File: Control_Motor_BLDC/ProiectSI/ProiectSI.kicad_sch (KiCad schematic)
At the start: 72 parts, among them J1 Screw_Terminal_01x05, J2 Conn_01x04_Pin, J3 Screw_Terminal_01x03, J5 Conn_01x02_Pin, Q1 NMOS_Substrate, Q2 NMOS_Substrate, Q3 NMOS_Substrate, Q4 NMOS_Substrate, Q5 NMOS_Substrate, Q6 NMOS_Substrate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

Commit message: Realizat layout PCB
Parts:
- J2: footprint Connector_PinHeader_1.00mm:PinHeader_1x04_P1.00mm_Horizontal -> Connector_PinHeader_1.00mm:PinHeader_1x04_P1.00mm_Vertical
- J5: footprint Connector_PinHeader_1.00mm:PinHeader_1x02_P1.00mm_Vertical_SMD_Pin1Left -> Connector_PinHeader_1.00mm:PinHeader_1x02_P1.00mm_Vertical
- Q1, Q2, Q3, Q4, Q5, Q6: footprint (none) -> Package_TO_SOT_THT:TO-220-3_Vertical
- R1: footprint (none) -> Resistor_SMD:R_0603_1608Metric
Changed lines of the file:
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@@
 			)
 		)
-		(property "Footprint" ""
+		(property "Footprint" "Package_TO_SOT_THT:TO-220-3_Vertical"
 			(at 89.535 212.09 0)
 			(effects
@@
 			)
 		)
-		(property "Footprint" ""
+		(property "Footprint" "Package_TO_SOT_THT:TO-220-3_Vertical"
 			(at 222.885 189.23 0)
 			(effects
@@
 			)
 		)
-		(property "Footprint" "Connector_PinHeader_1.00mm:PinHeader_1x04_P1.00mm_Horizontal"
+		(property "Footprint" "Connector_PinHeader_1.00mm:PinHeader_1x04_P1.00mm_Vertical"
 			(at 111.76 88.9 0)
 			(effects
@@
 			)
 		)
-		(property "Footprint" ""
+		(property "Footprint" "Package_TO_SOT_THT:TO-220-3_Vertical"
 			(at 222.885 213.36 0)
 			(effects
@@
 			)
 		)
-		(property "Footprint" ""
+		(property "Footprint" "Package_TO_SOT_THT:TO-220-3_Vertical"
 			(at 158.115 189.23 0)
 			(effects
@@
 			)
 		)
-		(property "Footprint" ""
+		(property "Footprint" "Resistor_SMD:R_0603_1608Metric"
 			(at 60.452 245.11 90)
 			(effects
@@
 			)
 		)
-		(property "Footprint" ""
+		(property "Footprint" "Package_TO_SOT_THT:TO-220-3_Vertical"
 			(at 89.535 187.96 0)
 			(effects
@@
 		(on_board yes)
 		(dnp no)
-		(fields_autoplaced yes)
 		(property "Reference" "SW1"
 			(at 101.6 43.18 0)
@@
 			)
 		)
-		(property "Footprint" ""
+		(property "Footprint" "Package_TO_SOT_THT:TO-220-3_Vertical"
 			(at 158.115 213.36 0)
 			(effects
@@
 			)
 		)
-		(property "Footprint" "Connector_PinHeader_1.00mm:PinHeader_1x02_P1.00mm_Vertical_SMD_Pin1Left"
+		(property "Footprint" "Connector_PinHeader_1.00mm:PinHeader_1x02_P1.00mm_Vertical"
 			(at 90.17 99.06 0)
 			(effects

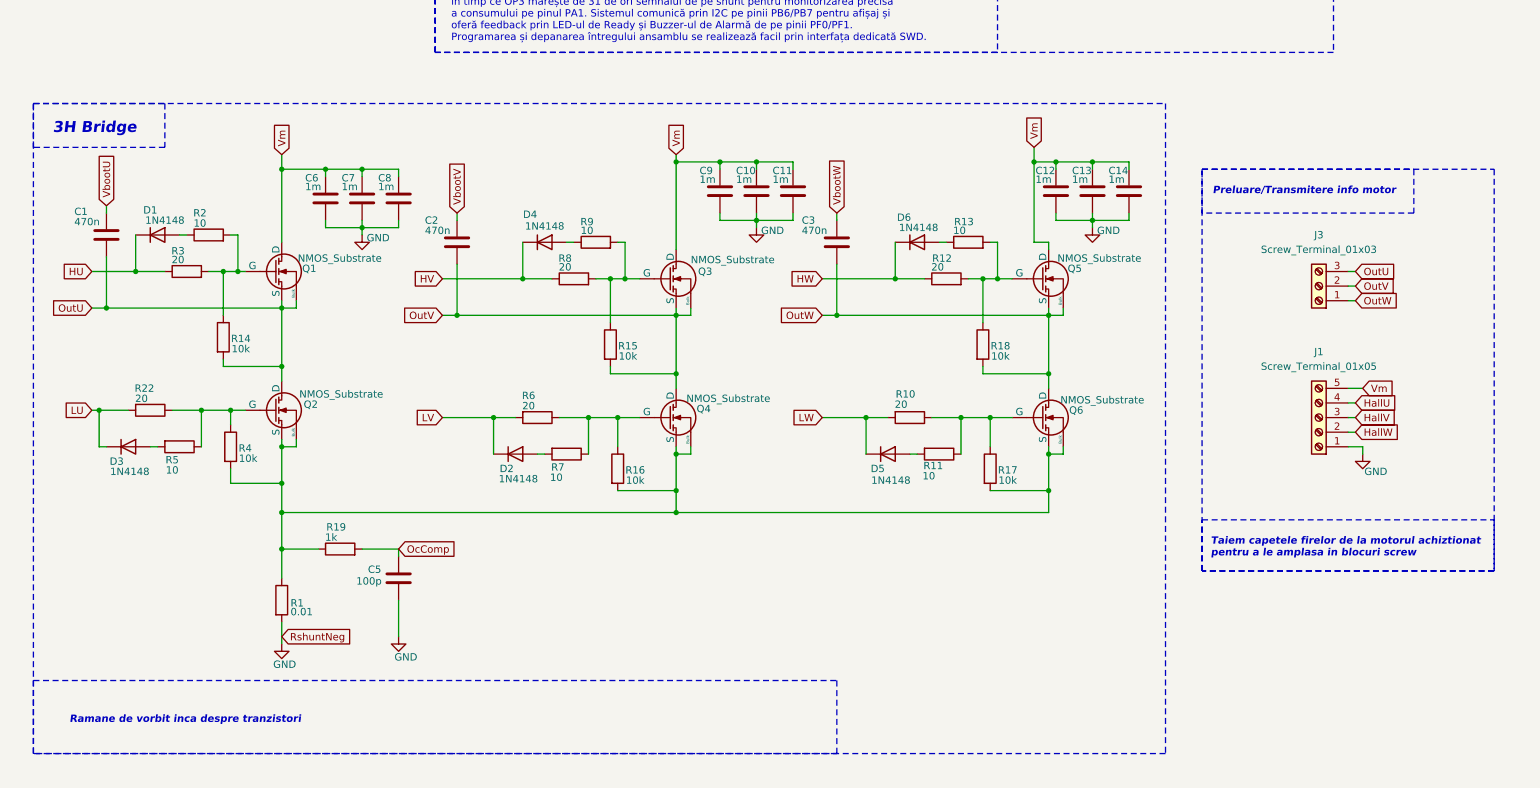
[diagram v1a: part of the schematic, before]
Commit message: Adaugat text informativ in schematic pentru puntea 3H
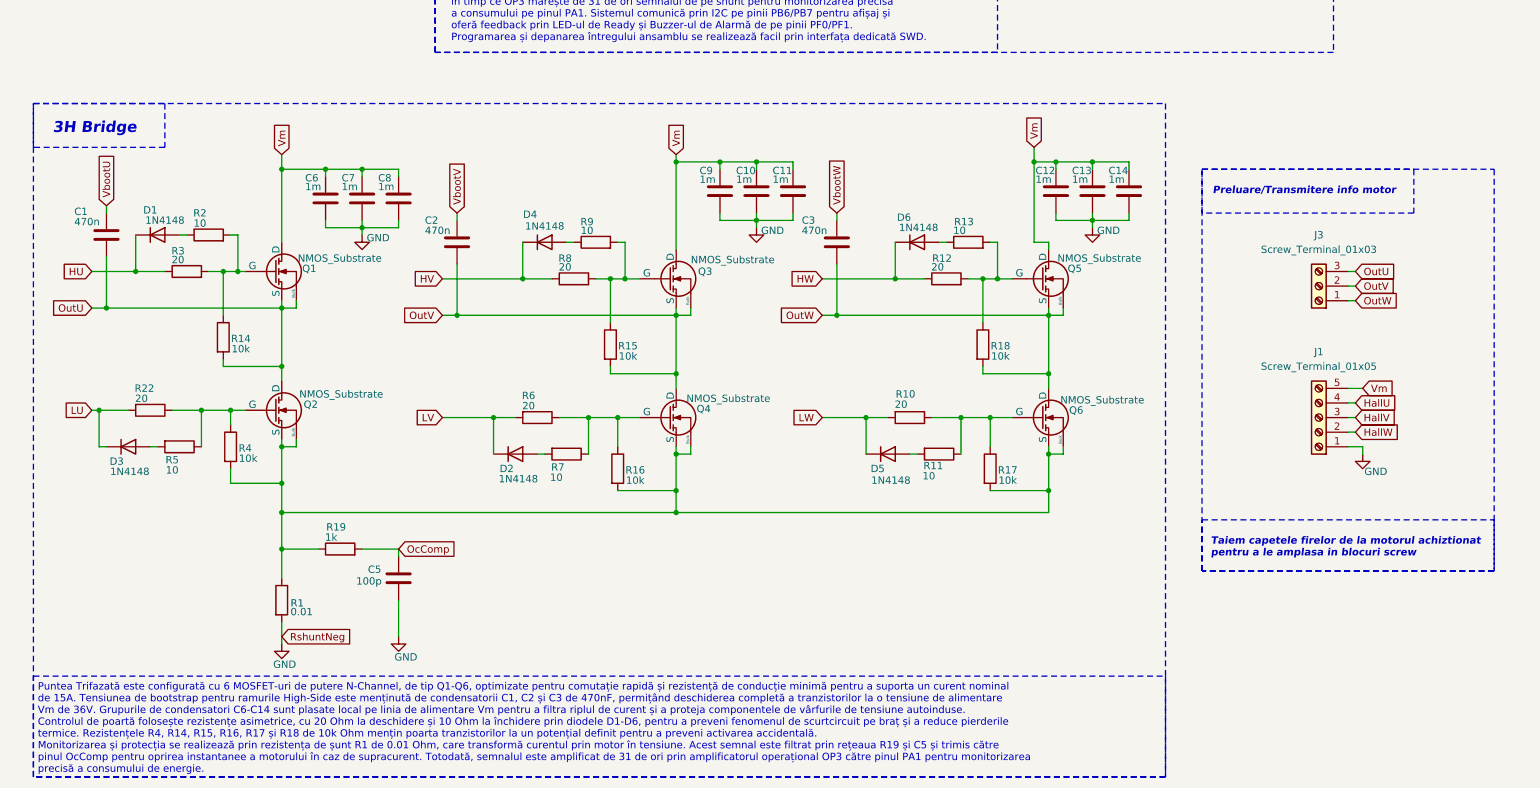
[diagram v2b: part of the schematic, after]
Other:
- note added: "Puntea Trifazată este configurată cu 6 MOSFET-uri de putere N-Channel, de tip Q1-Q6, optimizate pentru comutație rapidă și rezistență de conducție minimă pentru a suporta un curent nominal de 15A. Tensiunea de bootstrap pentru ramurile High-Side este menținută de condensatorii C1, C2 și C3 de 470nF, permițând deschiderea completă a tranzistorilor la o tensiune de alimentare Vm de 36V. Grupurile d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"
- note removed: "Ramane de vorbit inca despre tranzistori"
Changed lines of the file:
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@@
 	(rectangle
 		(start 19.05 158.75)
-		(end 215.9 271.78)
+		(end 215.9 275.844)
 		(stroke
 			(width 0)
@@
 	)
 	(rectangle
-		(start 19.05 259.08)
-		(end 158.75 271.78)
+		(start 19.05 258.318)
+		(end 215.9 275.844)
 		(stroke
 			(width 0)
@@
 		)
 	)
-	(text "Ramane de vorbit inca despre tranzistori "
+	(text "Puntea Trifazată este configurată cu 6 MOSFET-uri de putere N-Channel, de tip Q1-Q6, optimizate pentru comutație rapidă și rezistență de conducție minimă pentru a suporta un curent nominal \nde 15A. Tensiunea de bootstrap pentru ramurile High-Side este menținută de condensatorii C1, C2 și C3 de 470nF, permițând deschiderea completă a tranzistorilor la o tensiune de alimentare\nVm de 36V. Grupurile de condensatori C6-C14 sunt plasate local pe linia de alimentare Vm pentru a filtra riplul de curent și a proteja componentele de vârfurile de tensiune autoinduse.\nControlul de poartă folosește rezistențe asimetrice, cu 20 Ohm la deschidere și 10 Ohm la închidere prin diodele D1-D6, pentru a preveni fenomenul de scurtcircuit pe braț și a reduce pierderile\ntermice. Rezistențele R4, R14, R15, R16, R17 și R18 de 10k Ohm mențin poarta tranzistorilor la un potențial definit pentru a preveni activarea accidentală.\nMonitorizarea și protecția se realizează prin rezistența de șunt R1 de 0.01 Ohm, care transformă curentul prin motor în tensiune. Acest semnal este filtrat prin rețeaua R19 și C5 și trimis către\npinul OcComp pentru oprirea instantanee a motorului în caz de supracurent. Totodată, semnalul este amplificat de 31 de ori prin amplificatorul operațional OP3 către pinul PA1 pentru monitorizarea\nprecisă a consumului de energie."
 		(exclude_from_sim no)
-		(at 45.466 265.938 0)
+		(at 19.812 267.462 0)
 		(effects
 			(font
 				(size 1.27 1.27)
-				(thickness 0.254)
-				(bold yes)
-				(italic yes)
+				(thickness 0.1588)
 			)
+			(justify left)
 		)
 	)

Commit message: Adaugat clarificare schematic la punte
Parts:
- R23: value 30k -> 21k
- R24: value 1k -> 1.43k
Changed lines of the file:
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@@
 			(font
 				(size 1.905 1.905)
-				(thickness 0.381)
-				(bold yes)
-				(italic yes)
+				(thickness 0.2381)
 			)
 		)
@@
 			)
 		)
-		(property "Value" "1k"
-			(at 211.836 118.364 90)
+		(property "Value" "1.43k"
+			(at 213.106 118.364 90)
 			(effects
 				(font
@@
 			)
 		)
-		(property "Value" "30k"
+		(property "Value" "21k"
 			(at 201.93 118.618 90)
 			(effects

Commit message: Modificare proiecte
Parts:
- removed BZ1: Buzzer, Buzzer_Beeper:Buzzer_TDK_PS1240P02BT_D12.2mm_H6.5mm, symbol Device:Buzzer
- removed C19: 7.96n, Capacitor_SMD:C_0603_1608Metric, symbol Device:C
- removed D8: LED, LED_SMD:LED_0805_2012Metric, symbol Device:LED
- removed Q1, Q2, Q3, Q4, Q5, Q6: NMOS_Substrate, Package_TO_SOT_THT:TO-220-3_Vertical, symbol Simulation_SPICE:NMOS_Substrate
- removed R11, R13, R2, R5, R7, R9: 10, Resistor_SMD:R_0603_1608Metric, symbol Device:R
- removed R25: 130, Resistor_SMD:R_0603_1608Metric, symbol Device:R
- removed U2, U3: DRV5055A2xDBZxQ1, Package_TO_SOT_SMD:SOT-23, symbol Sensor_Magnetic:DRV5055A2xDBZxQ1
- added BZ2: Buzzer, Buzzer_Beeper:Buzzer_TDK_PS1240P02BT_D12.2mm_H6.5mm, symbol Device:Buzzer
- added C21, C22: 1u, Capacitor_SMD:C_0603_1608Metric, symbol Device:C
- added C23: 100nF, Capacitor_SMD:C_0603_1608Metric, symbol Device:C
- added D9: LED, LED_SMD:LED_0805_2012Metric, symbol Device:LED
- added Maneta_Accel1, Maneta_Frana1: Conn_01x03, Connector_PinHeader_2.54mm:PinHeader_1x03_P2.54mm_Vertical, symbol Connector_Generic:Conn_01x03
- added Q10, Q11, Q12, Q7, Q8, Q9: RD3L150SNTL1, RD3L150SNTL:RD3P175SNFRATL, symbol RD3L150SNTL1:RD3L150SNTL1
- added Q13, Q14: BC846B, symbol BC846B:BC846B
- added R28, R30: 10k, Resistor_SMD:R_0603_1608Metric, symbol Device:R
- added R_sig1, R_sig2: 100k, Resistor_SMD:R_0603_1608Metric, symbol Device:R
- C20: value 7.96n -> 100nF
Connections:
- net Accel: now also C23.1, R_sig1.2
- net Frana: now also R_sig2.2
- net GND: now also C21.2, C22.2, C23.2, Maneta_Accel1.3 (Pin_3), Maneta_Frana1.3 (Pin_3), Q13.2, Q14.2, R_sig1.1, R_sig2.1; no longer SW1.1 (C), U1.7 (NRST)
- net OutU: now also Q10.2 (D), Q7.3 (S)
- net OutV: now also Q11.2 (D), Q8.3 (S)
- net OutW: now also Q12.2 (D), Q9.3 (S)
- net VDD: now also BZ2.1 (+), C21.1, C22.1, D9.2 (A), Maneta_Accel1.1 (Pin_1), Maneta_Frana1.1 (Pin_1)
- net Vm: now also Q7.2 (D), Q8.2 (D), Q9.2 (D)
- net at R1.1, R16.2, R17.2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: now also Q10.3 (S), Q11.3 (S), Q12.3 (S)
- net at R22.1, R4.1: now also D3.2 (A), Q10.1 (G)
- net at R10.1, R17.1: now also D5.2 (A), Q12.1 (G)
- net Buzer_control: now reaches U1.5 (PF1)
- net Buzer_control: now also R30.2
- net at R12.2, R18.1: now also D6.2 (A), Q9.1 (G)
- net at R20.1: now also Maneta_Accel1.2 (Pin_2)
- net at R14.1, R3.2: now also D1.2 (A), Q7.1 (G)
- net at R15.1, R8.2: now also D4.2 (A), Q8.1 (G)
- net Led_control: now reaches U1.4 (PF0)
- net Led_control: now also R28.1
- net at R16.1, R6.1: now also D2.2 (A), Q11.1 (G)
- net at R21.1: now also Maneta_Frana1.2 (Pin_2)
- new net: Q13.1, R28.2
- new net: SW1.1 (C), U1.7 (NRST)
- new net: D9.1 (K), Q13.3
- new net: Q14.1, R30.1
- new net: BZ2.2 (-), Q14.3
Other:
- note added: "Preluare semnal analogic de la manete (potențiometre). Filtru RC trece-jos (1kΩ + 100nF) pentru atenuarea zgomotului. Include rezistențe pull-down de 100kΩ pentru siguranță (fail-safe la ruperea cablului). Se recomandă cabluri ecranate spre manete pentru imunitate la zgomot (EMI)."
- note added: "SQJ148EP-T1_GE3"
- note removed: "Preluare tensiuni de la manete care sunt tot niste senzori hall, obligatoriu cabluri ecranate de la maneta pana la motor (EMI). RC, fc=20k conform datasheet"
- moved on the sheet: D2, D3, D5, R10, R22, R4, R6
